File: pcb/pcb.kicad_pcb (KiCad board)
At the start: 2 copper layers, 75 x 75 mm, 25 parts, among them U1 1117-3.3, U2 NORTH, U3 SOUTH, U4 EAST, U5 WEST, U6 RP2040

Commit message: update pcb
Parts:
- added C15: 0.1uF, Capacitor_SMD:C_0201_0603Metric, F.Cu at (19.6, 58.8)
- added R5: 10k, Resistor_SMD:R_0201_0603Metric, F.Cu at (26.6, 59.6)
- added R6: 1k, Resistor_SMD:R_0201_0603Metric, F.Cu at (23.0, 68.0)
- added U7: ~, Andrews_Library:LCSC_W25Q16JVSSIQ_C131025, F.Cu at (8.52, 65.8)
- added U8: ~, Andrews_Library:LCSC_TS-1089S-02526_C455282, F.Cu at (8.67, 54.8)
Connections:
- U6 pad 51: unconnected-(U6-QSPI_SD3-Pad51) -> QSPI_SD3
- U6 pad 52: unconnected-(U6-QSPI_SCLK-Pad52) -> QSPI_SCLK
- U6 pad 53: unconnected-(U6-QSPI_SD0-Pad53) -> QSPI_SD0
- U6 pad 54: unconnected-(U6-QSPI_SD2-Pad54) -> QSPI_SD2
- U6 pad 55: unconnected-(U6-QSPI_SD1-Pad55) -> QSPI_SD1
- U6 pad 56: unconnected-(U6-~{QSPI_SS}-Pad56) -> QSPI_SS

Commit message: working on pcb
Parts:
- moved C15 13.1 mm to (6.62, 60.2), turned to 90 degrees
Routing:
- net +3V3: track 12.4 -> 14.0 mm
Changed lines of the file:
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@@
 	(footprint "Capacitor_SMD:C_0201_0603Metric"
 		(layer "F.Cu")
-		(at 19.6 58.825)
+		(at 6.615 60.245 90)
 		(descr "Capacitor SMD 0201 (0603 Metric), square (rectangular) end terminal, IPC-7351 nominal, (Body size source: https://www.vishay.com/docs/20052/crcw0201e3.pdf)")
 		(tags "capacitor")
 		(property "Reference" "C15"
-			(at 0 -1.05 0)
+			(at 0 -1.05 90)
 			(layer "F.SilkS")
+			(hide yes)
 			(effects
 				(font
@@
 		)
 		(property "Value" "0.1uF"
-			(at 0 1.05 0)
+			(at 0 1.05 90)
 			(layer "F.Fab")
+			(hide yes)
 			(effects
 				(font
@@
 		)
 		(property "Datasheet" ""
-			(at 0 0 0)
+			(at 0 0 90)
 			(layer "F.Fab")
 			(hide yes)
@@
 		)
 		(property "Description" "Unpolarized capacitor"
-			(at 0 0 0)
+			(at 0 0 90)
 			(layer "F.Fab")
 			(hide yes)
@@
 		)
 		(property "KiLib_Generator" "SMD_2terminal_chip_molded"
-			(at 0 0 0)
+			(at 0 0 90)
 			(layer "F.SilkS")
 			(hide yes)
@@
 		)
 		(property "LCSC" "C1591"
-			(at 0 0 0)
+			(at 0 0 90)
 			(unlocked yes)
 			(layer "F.Fab")
@@
 		)
 		(fp_text user "${REFERENCE}"
-			(at 0 -0.68 0)
+			(at 0 0 90)
 			(layer "F.Fab")
 			(effects
@@
 		)
 		(pad "" smd roundrect
-			(at -0.345 0)
+			(at -0.345 0 90)
 			(size 0.318 0.36)
 			(layers "F.Paste")
@@
 		)
 		(pad "" smd roundrect
-			(at 0.345 0)
+			(at 0.345 0 90)
 			(size 0.318 0.36)
 			(layers "F.Paste")
@@
 		)
 		(pad "1" smd roundrect
-			(at -0.32 0)
+			(at -0.32 0 90)
 			(size 0.46 0.4)
 			(layers "F.Cu" "F.Mask")
@@
 		)
 		(pad "2" smd roundrect
-			(at 0.32 0)
+			(at 0.32 0 90)
 			(size 0.46 0.4)
 			(layers "F.Cu" "F.Mask")
@@
 		(sheetname "/")
 		(sheetfile "pcb.kicad_sch")
-		(units
-			(unit
-				(name "A")
-				(pins "1" "6" "8" "4" "5" "7" "2" "3")
-			)
-		)
 		(attr smd)
 		(duplicate_pad_numbers_are_jumpers no)
@@
 			(layer "F.SilkS")
 		)
+		(fp_circle
+			(center -2 2)
+			(end -1.75 2)
+			(stroke
+				(width 0.1)
+				(type solid)
+			)
+			(fill yes)
+			(layer "F.SilkS")
+		)
 		(fp_text user "${REFERENCE}"
 			(at 0 0 0)
@@
 			)
 		)
-		(point
-			(at 6.52 67.825)
-			(size 1)
-			(layer "F.SilkS")
-		)
 		(pad "1" smd roundrect
 			(at -1.905 3.625)
@@
 		(layer "F.Cu")
 		(net "+3V3")
+	)
+	(segment
+		(start 6.615 60.565)
+		(end 6.615 62.2)
+		(width 0.4)
+		(layer "F.Cu")
+		(net "+3V3")

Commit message: working on pcb
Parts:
- moved R5 22.4 mm to (5.00, 65.8), turned to -90 degrees
- moved R6 16.7 mm to (6.62, 71.2), turned to -90 degrees
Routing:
- net QSPI_SS: track 0.00 -> 3.97 mm
- net +3V3: track 14.0 -> 18.0 mm
- net Net-(U8-IN1): track 0.00 -> 2.17 mm
- net GND: track 19.1 -> 19.9 mm, vias 19 -> 22
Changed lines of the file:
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@@
 	(footprint "Resistor_SMD:R_0201_0603Metric"
 		(layer "F.Cu")
-		(at 23.045 68)
+		(at 6.615 71.155 -90)
 		(descr "Resistor SMD 0201 (0603 Metric), square (rectangular) end terminal, IPC-7351 nominal, (Body size source: https://www.vishay.com/docs/20052/crcw0201e3.pdf)")
 		(tags "resistor")
 		(property "Reference" "R6"
-			(at 0 -1.05 0)
+			(at 0 -1.05 90)
 			(layer "F.SilkS")
+			(hide yes)
 			(effects
 				(font
@@
 		)
 		(property "Value" "1k"
-			(at 0 1.05 0)
+			(at 0 1.05 90)
 			(layer "F.Fab")
+			(hide yes)
 			(effects
 				(font
@@
 		)
 		(property "Datasheet" ""
-			(at 0 0 0)
+			(at 0 0 90)
 			(layer "F.Fab")
 			(hide yes)
@@
 		)
 		(property "Description" "Resistor"
-			(at 0 0 0)
+			(at 0 0 90)
 			(layer "F.Fab")
 			(hide yes)
@@
 		)
 		(property "KiLib_Generator" "SMD_2terminal_chip_molded"
-			(at 0 0 0)
+			(at 0 0 90)
 			(layer "F.SilkS")
 			(hide yes)
@@
 		)
 		(property "LCSC" "C22548"
-			(at 0 0 0)
+			(at 0 0 270)
 			(unlocked yes)
 			(layer "F.Fab")
@@
 		)
 		(fp_text user "${REFERENCE}"
-			(at 0 -0.68 0)
+			(at 0 0 90)
 			(layer "F.Fab")
 			(effects
@@
 		)
 		(pad "" smd roundrect
-			(at -0.345 0)
+			(at -0.345 0 270)
 			(size 0.318 0.36)
 			(layers "F.Paste")
@@
 		)
 		(pad "" smd roundrect
-			(at 0.345 0)
+			(at 0.345 0 270)
 			(size 0.318 0.36)
 			(layers "F.Paste")
@@
 		)
 		(pad "1" smd roundrect
-			(at -0.32 0)
+			(at -0.32 0 270)
 			(size 0.46 0.4)
 			(layers "F.Cu" "F.Mask")
@@
 		)
 		(pad "2" smd roundrect
-			(at 0.32 0)
+			(at 0.32 0 270)
 			(size 0.46 0.4)
 			(layers "F.Cu" "F.Mask")
@@
 	(footprint "Resistor_SMD:R_0201_0603Metric"
 		(layer "F.Cu")
-		(at 26.575 59.625)
+		(at 5 65.825 -90)
 		(descr "Resistor SMD 0201 (0603 Metric), square (rectangular) end terminal, IPC-7351 nominal, (Body size source: https://www.vishay.com/docs/20052/crcw0201e3.pdf)")
 		(tags "resistor")
 		(property "Reference" "R5"
-			(at 0 -1.05 0)
+			(at 0 -1.05 90)
 			(layer "F.SilkS")
+			(hide yes)
 			(effects
 				(font
@@
 		)
 		(property "Value" "10k"
-			(at 0 1.05 0)
+			(at 0 1.05 90)
 			(layer "F.Fab")
+			(hide yes)
 			(effects
 				(font
@@
 		)
 		(property "Datasheet" ""
-			(at 0 0 0)
+			(at 0 0 90)
 			(layer "F.Fab")
 			(hide yes)
@@
 		)
 		(property "Description" "Resistor"
-			(at 0 0 0)
+			(at 0 0 90)
 			(layer "F.Fab")
 			(hide yes)
@@
 		)
 		(property "KiLib_Generator" "SMD_2terminal_chip_molded"
-			(at 0 0 0)
+			(at 0 0 90)
 			(layer "F.SilkS")
 			(hide yes)
@@
 		)
 		(property "LCSC" "C98220"
-			(at 0 0 0)
+			(at 0 0 270)
 			(unlocked yes)
 			(layer "F.Fab")
@@
 		)
 		(fp_text user "${REFERENCE}"
-			(at 0 -0.68 0)
+			(at 0 0 90)
 			(layer "F.Fab")
 			(effects
@@
 		)
 		(pad "" smd roundrect
-			(at -0.345 0)
+			(at -0.345 0 270)
 			(size 0.318 0.36)
 			(layers "F.Paste")
@@
 		)
 		(pad "" smd roundrect
-			(at 0.345 0)
+			(at 0.345 0 270)
 			(size 0.318 0.36)
 			(layers "F.Paste")
@@
 		)
 		(pad "1" smd roundrect
-			(at -0.32 0)
+			(at -0.32 0 270)
 			(size 0.46 0.4)
 			(layers "F.Cu" "F.Mask")
@@
 		)
 		(pad "2" smd roundrect
-			(at 0.32 0)
+			(at 0.32 0 270)
 			(size 0.46 0.4)
 			(layers "F.Cu" "F.Mask")
@@
 		(sheetname "/")
 		(sheetfile "pcb.kicad_sch")
-		(units
-			(unit
-				(name "A")
-				(pins "1" "2" "3" "4")
-			)
-		)
 		(attr smd)
 		(duplicate_pad_numbers_are_jumpers no)
@@
 		)
 		(pad "1" smd roundrect
-			(at -2.15 -1.085)
+			(at 2.15 1.085)
 			(size 1.3 0.73)
 			(layers "F.Cu" "F.Mask" "F.Paste")
@@
 		)
 		(pad "4" smd roundrect
-			(at 2.15 1.085)
+			(at -2.15 -1.085)
 			(size 1.3 0.73)
 			(layers "F.Cu" "F.Mask" "F.Paste")
@@
 	)
 	(segment
+		(start 6.615 59.925)
+		(end 6.615 59.1)
+		(width 0.4)
+		(layer "F.Cu")
+		(net "GND")
+	)
+	(segment
 		(start 13.75 9.82)
 		(end 13.75 10.75)
@@
 	)
 	(via
+		(at 6.52 53.725)
+		(size 0.6)
+		(drill 0.3)
+		(layers "F.Cu" "B.Cu")
+		(net "GND")
+	)
+	(via
 		(at 13.75 10.75)
 		(size 0.6)
@@
 	)
 	(via
+		(at 6.52 55.895)
+		(size 0.6)
+		(drill 0.3)
+		(layers "F.Cu" "B.Cu")
+		(net "GND")
+	)
+	(via
 		(at 54.5 44)
 		(size 0.6)
@@
 	)
 	(via
+		(at 6.615 59.1)
+		(size 0.6)
+		(drill 0.3)
+		(layers "F.Cu" "B.Cu")
+		(net "GND")
+	)
+	(via
 		(at 60.25 21.425)
 		(size 0.6)
@@
 	)
 	(segment
+		(start 5 65.505)
+		(end 5 63.815)
+		(width 0.4)
+		(layer "F.Cu")
+		(net "+3V3")
+	)
+	(segment
 		(start 38.1 40.3)
 		(end 38.4 40)
@@
 	)
 	(segment
+		(start 5 63.815)
+		(end 6.615 62.2)
+		(width 0.4)
+		(layer "F.Cu")
+		(net "+3V3")
+	)
+	(segment
 		(start 39.5 40)
 		(end 39.8 39.7)
@@
 	)
 	(segment
+		(start 5 67.835)
+		(end 6.615 69.45)
+		(width 0.4)
+		(layer "F.Cu")
+		(net "QSPI_SS")
+	)
+	(segment
+		(start 5 66.145)
+		(end 5 67.835)
+		(width 0.4)
+		(layer "F.Cu")
+		(net "QSPI_SS")
+	)
+	(segment
+		(start 10.82 53.725)
+		(end 10.82 55.895)
+		(width 0.73)
+		(layer "F.Cu")
+		(net "Net-(U8-IN1)")
+	)
+	(segment
 		(start 13.75 9.18)
 		(end 13.75 7.5)
@@
 		)
 	)
+	(group ""
+		(members "2cb71cbe-b98c-49a1-91f3-c4075b89a021" "39d55563-e15e-45ca-9a0f-27c0f16a8ed3"
+			"60269061-dd71-4ace-8a2f-56b316d2844d" "61ee9c33-24cf-48a5-8685-db579f4fdd16"
+		)
+	)

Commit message: lots of pcb work
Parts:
- moved C15 38.1 mm to (25.3, 27.0)
- moved R5 38.1 mm to (23.7, 32.6)
- moved R6 38.1 mm to (25.3, 38.0)
- moved U7 38.1 mm to (27.2, 32.6)
- moved C5 27.6 mm to (41.6, 32.3), turned to 90 degrees
- moved C4 27.5 mm to (40.9, 32.3), turned to 90 degrees
- moved C3 27.4 mm to (40.1, 32.3), turned to 90 degrees
- moved U8 23.4 mm to (27.5, 40.8), turned to 180 degrees
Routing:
- net USB_DP: track 0.00 -> 38.0 mm
- net USB_DN: track 0.00 -> 37.7 mm
- net +3V3: track 18.0 -> 53.1 mm
- net QSPI_SD3: track 0.00 -> 14.4 mm
- net QSPI_SCLK: track 0.00 -> 12.3 mm
- net QSPI_SD0: track 0.00 -> 9.99 mm
- net Net-(U8-IN1): track 2.17 -> 3.65 mm
- net +1V1: track 1.50 -> 2.90 mm
- net QSPI_SS: track 3.97 -> 5.36 mm

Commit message: more routing
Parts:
- moved C3 0.60 mm to (40.7, 32.3)
- moved C4 0.60 mm to (41.5, 32.3)
- moved C5 0.60 mm to (42.2, 32.3)
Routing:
- net +3V3: track 53.1 -> 65.3 mm
- net +1V1: track 2.90 -> 6.38 mm
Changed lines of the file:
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@@
 	(footprint "Capacitor_SMD:C_0201_0603Metric"
 		(layer "F.Cu")
-		(at 40.85 32.345 90)
+		(at 41.45 32.345 90)
 		(descr "Capacitor SMD 0201 (0603 Metric), square (rectangular) end terminal, IPC-7351 nominal, (Body size source: https://www.vishay.com/docs/20052/crcw0201e3.pdf)")
 		(tags "capacitor")
@@
 	(footprint "Capacitor_SMD:C_0201_0603Metric"
 		(layer "F.Cu")
-		(at 41.6 32.345 90)
+		(at 42.2 32.345 90)
 		(descr "Capacitor SMD 0201 (0603 Metric), square (rectangular) end terminal, IPC-7351 nominal, (Body size source: https://www.vishay.com/docs/20052/crcw0201e3.pdf)")
 		(tags "capacitor")
@@
 	(footprint "Capacitor_SMD:C_0201_0603Metric"
 		(layer "F.Cu")
-		(at 40.1 32.345 90)
+		(at 40.7 32.345 90)
 		(descr "Capacitor SMD 0201 (0603 Metric), square (rectangular) end terminal, IPC-7351 nominal, (Body size source: https://www.vishay.com/docs/20052/crcw0201e3.pdf)")
 		(tags "capacitor")
@@
 	)
 	(segment
-		(start 41.6 32.025)
-		(end 39.35 32.025)
+		(start 42.2 32.025)
+		(end 39.95 32.025)
 		(width 0.4)
 		(layer "F.Cu")
@@
 	)
 	(via
-		(at 39.35 32.025)
+		(at 39.95 32.025)
 		(size 0.6)
 		(drill 0.3)
@@
 	)
 	(segment
-		(start 34.59636 38.5)
-		(end 34.0625 38.5)
-		(width 0.2)
-		(layer "F.Cu")
-		(net "+3V3")
-	)
-	(segment
 		(start 37.7 40.9375)
 		(end 38.1 40.9375)
@@
 	)
 	(segment
-		(start 39.7 34.0625)
-		(end 39.7 34.59636)
+		(start 34.59636 38.5)
+		(end 34.0625 38.5)
 		(width 0.2)
 		(layer "F.Cu")
@@
 	)
 	(segment
-		(start 38.1 40.3)
-		(end 38.4 40)
+		(start 35.09909 39.59909)
+		(end 35.09909 38.79909)
 		(width 0.2)
 		(layer "F.Cu")
@@
 	)
 	(segment
-		(start 39.3 34.0625)
-		(end 39.3 34.59636)
+		(start 38.1 40.3)
+		(end 38.4 40)
 		(width 0.2)
 		(layer "F.Cu")
@@
 	)
 	(segment
+		(start 37.7 40.9375)
+		(end 37.7 40.40364)
+		(width 0.2)
+		(layer "F.Cu")
+		(net "+3V3")
+	)
+	(segment
 		(start 37.3 34.59636)
 		(end 36.99636 34.9)
@@
 	)
 	(segment
+		(start 39.8 35.5)
+		(end 39.8 38.8)
+		(width 0.2)
+		(layer "F.Cu")
+		(net "+3V3")
+	)
+	(segment
 		(start 39.3 34.0625)
 		(end 39.7 34.0625)
@@
 	)
 	(segment
-		(start 39.7 34.59636)
-		(end 40.00364 34.9)
+		(start 40.4 34.9)
+		(end 39.8 35.5)
 		(width 0.2)
 		(layer "F.Cu")
@@
 	)
 	(segment
+		(start 42.9 31.5)
+		(end 42.9 34)
+		(width 0.2)
+		(layer "F.Cu")
+		(net "+3V3")
+	)
+	(segment
 		(start 39.8 38.8)
 		(end 40.00364 38.59636)
@@
 	)
 	(segment
-		(start 32.768628 27.5)
-		(end 26.8 27.5)
+		(start 37.29636 40)
+		(end 35.5 40)
 		(width 0.2)
 		(layer "F.Cu")
@@
 	)
 	(segment
-		(start 37.7 34.59636)
-		(end 37.7 34.0625)
+		(start 32.768628 27.5)
+		(end 26.8 27.5)
 		(width 0.2)
 		(layer "F.Cu")
@@
 	)
 	(segment
-		(start 34.8 35.10364)
-		(end 34.8 38.29636)
+		(start 35.09909 38.79909)
+		(end 34.8 38.5)
 		(width 0.2)
 		(layer "F.Cu")
@@
 	)
 	(segment
-		(start 40.00364 34.9)
-		(end 40.9375 34.9)
+		(start 34.8 35.10364)
+		(end 34.8 38.29636)
 		(width 0.2)
 		(layer "F.Cu")
@@
 	)
 	(segment
-		(start 39.09636 34.8)
-		(end 37.90364 34.8)
+		(start 40.9375 34.9)
+		(end 40.4 34.9)
 		(width 0.2)
 		(layer "F.Cu")
@@
 	)
 	(segment
+		(start 39.3 34.0625)
+		(end 39.3 31.826471)
+		(width 0.2)
+		(layer "F.Cu")
+		(net "+3V3")
+	)
+	(segment
 		(start 40.1 38.5)
 		(end 40.9375 38.5)
@@
 	)
 	(segment
-		(start 38.1 40.9375)
-		(end 38.1 40.3)
+		(start 35.5 40)
+		(end 35.09909 39.59909)
 		(width 0.2)
 		(layer "F.Cu")
@@
 	)
 	(segment
-		(start 40.00364 34.9)
-		(end 40.00364 38.59636)
+		(start 38.1 40.9375)
+		(end 38.1 40.3)
 		(width 0.2)
 		(layer "F.Cu")
@@
 	)
 	(segment
+		(start 42.9 34)
+		(end 42 34.9)
+		(width 0.2)
+		(layer "F.Cu")
+		(net "+3V3")
+	)
+	(segment
+		(start 37.7 40.40364)
+		(end 37.29636 40)
+		(width 0.2)
+		(layer "F.Cu")
+		(net "+3V3")
+	)
+	(segment
 		(start 38.4 40)
 		(end 39.5 40)
@@
 	)
 	(segment
-		(start 39.3 34.59636)
-		(end 39.09636 34.8)
+		(start 42 34.9)
+		(end 40.9375 34.9)
+		(width 0.2)
+		(layer "F.Cu")
+		(net "+3V3")
+	)
+	(segment
+		(start 34.8 38.5)
+		(end 34.59636 38.5)
+		(width 0.2)
+		(layer "F.Cu")
+		(net "+3V3")
+	)
+	(segment
+		(start 39.3 31.826471)
+		(end 39.926471 31.2)
 		(width 0.2)
 		(layer "F.Cu")
@@
 	)
 	(segment
-		(start 36.99636 34.9)
-		(end 34.0625 34.9)
+		(start 42.6 31.2)
+		(end 42.9 31.5)
 		(width 0.2)
 		(layer "F.Cu")
@@
 	)
 	(segment
-		(start 37.3 34.0625)
-		(end 37.7 34.0625)
+		(start 36.99636 34.9)
+		(end 34.0625 34.9)
 		(width 0.2)
 		(layer "F.Cu")
@@
 	)
 	(segment
-		(start 37.90364 34.8)
-		(end 37.7 34.59636)
+		(start 37.3 34.0625)
+		(end 37.7 34.0625)
 		(width 0.2)
 		(layer "F.Cu")
@@
 	)
 	(segment
+		(start 39.926471 31.2)
+		(end 42.6 31.2)
+		(width 0.2)
+		(layer "F.Cu")
+		(net "+3V3")
+	)
+	(segment
 		(start 39.5 40)
 		(end 39.8 39.7)
@@
 	)
 	(segment
-		(start 40.1 32.665)
-		(end 41.6 32.665)
+		(start 40.1 34.0625)
+		(end 40.1 33.265)
+		(width 0.2)
+		(layer "F.Cu")
+		(net "+1V1")
+	)
+	(segment
+		(start 40.1 34.59636)
+		(end 39.89636 34.8)
+		(width 0.2)
+		(layer "F.Cu")
+		(net "+1V1")
+	)
+	(segment
+		(start 40.7 32.665)
+		(end 42.2 32.665)
 		(width 0.4)
 		(layer "F.Cu")
@@
 	(segment
 		(start 40.1 34.0625)
-		(end 40.1 32.665)
+		(end 40.1 34.59636)
+		(width 0.2)
+		(layer "F.Cu")
+		(net "+1V1")
+	)
+	(segment
+		(start 38.30364 34.8)
+		(end 38.1 34.59636)
+		(width 0.2)
+		(layer "F.Cu")
+		(net "+1V1")
+	)
+	(segment
+		(start 40.1 33.265)
+		(end 40.7 32.665)
+		(width 0.2)
+		(layer "F.Cu")
+		(net "+1V1")
+	)
+	(segment
+		(start 38.1 34.59636)
+		(end 38.1 34.0625)
+		(width 0.2)
+		(layer "F.Cu")
+		(net "+1V1")
+	)
+	(segment
+		(start 39.89636 34.8)
+		(end 38.30364 34.8)
 		(width 0.2)
 		(layer "F.Cu")

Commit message: even more pcb stuff
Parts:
- U2, U4: footprint Andrews_Library:DDR_CONTACT -> Andrews_Library:DDR_CONTACT_MIRROR
- moved C2 44.1 mm to (20.7, 4.05), turned to 90 degrees
- moved C1 39.9 mm to (23.0, 4.05), turned to -90 degrees
- moved U1 38.4 mm to (23.0, 6.05), turned to 180 degrees
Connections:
- U2 pad 2: unconnected-(U2-GPIO-Pad2) -> GPIO-25
- U5 pad 2: unconnected-(U5-GPIO-Pad2) -> GPIO-12
- U6 pad 15: unconnected-(U6-GPIO12-Pad15) -> GPIO-12
- U6 pad 37: unconnected-(U6-GPIO25-Pad37) -> GPIO-25
- U7 pad 4: unconnected-(U7-GND-Pad4) -> GND
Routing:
- net GPIO-25: track 0.00 -> 17.9 mm
- net GPIO-12: track 0.00 -> 16.2 mm
- net QSPI_SS: track 5.36 -> 17.0 mm
- net QSPI_SD1: track 0.00 -> 11.3 mm
- net VBUS: track 14.8 -> 25.3 mm
- net QSPI_SD2: track 0.00 -> 10.2 mm
- net GND: vias 22 -> 23

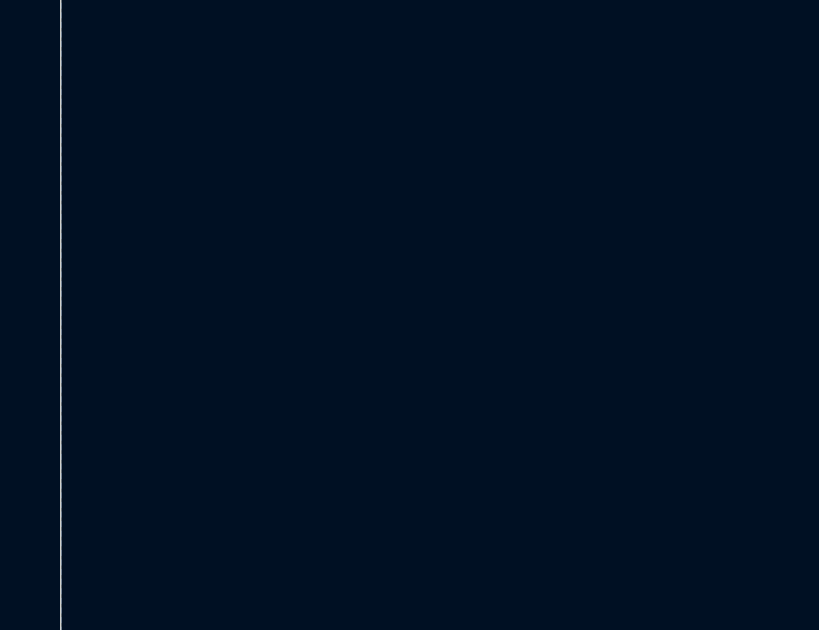
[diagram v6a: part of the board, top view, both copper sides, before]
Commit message: fix footprint
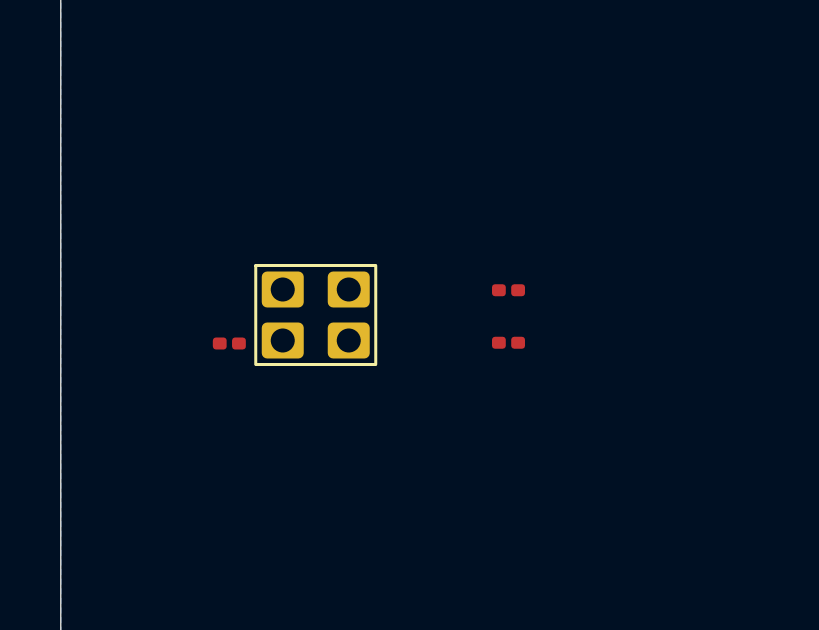
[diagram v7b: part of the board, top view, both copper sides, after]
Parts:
- added C16: 15pF, Capacitor_SMD:C_0201_0603Metric, F.Cu at (5.62, 61.6)
- added C17: 15pF, Capacitor_SMD:C_0201_0603Metric, F.Cu at (14.9, 59.8)
- added R7: 1k, Resistor_SMD:R_0201_0603Metric, F.Cu at (14.9, 61.6)
- added U9: ~, Andrews_Library:LCSC_X322512MSB4SI_C9002, F.Cu at (8.50, 60.6)
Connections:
- U6 pad 20: unconnected-(U6-XIN-Pad20) -> XIN
- U6 pad 21: unconnected-(U6-XOUT-Pad21) -> XOUT

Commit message: work on pcb
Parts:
- moved C16 30.6 mm to (33.8, 49.7)
- moved U9 29.0 mm to (34.2, 47.1), turned to 90 degrees
- moved C17 23.9 mm to (33.3, 44.6)
- moved R7 23.7 mm to (35.4, 49.7), turned to 180 degrees
- moved C10 1.29 mm to (38.7, 43.0)
- moved C6 1.29 mm to (38.7, 46.0)
- moved C7 1.29 mm to (38.7, 45.3)
- moved C8 1.29 mm to (38.7, 44.5)
- moved C9 1.29 mm to (38.7, 43.8)
- moved C11 1.29 mm to (40.1, 46.0)
- moved C12 1.29 mm to (40.1, 45.3)
- moved C13 1.29 mm to (40.1, 44.5)
- moved C14 1.29 mm to (40.1, 43.8)
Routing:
- net XOUT: track 0.00 -> 9.41 mm
- net XIN: track 0.00 -> 8.29 mm
- net Net-(C16-Pad1): track 0.00 -> 3.30 mm
- net GND: track 19.9 -> 21.5 mm, vias 23 -> 27
- net +3V3: track 65.3 -> 66.6 mm
